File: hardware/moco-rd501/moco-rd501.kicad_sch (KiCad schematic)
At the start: 34 parts, among them J1 Conn_01x06, J2 Debug, J3 Conn_01x02, J4 Conn_01x09, SW1 SW_Push, SW2 SW_Push, U1 XC6220B331MR

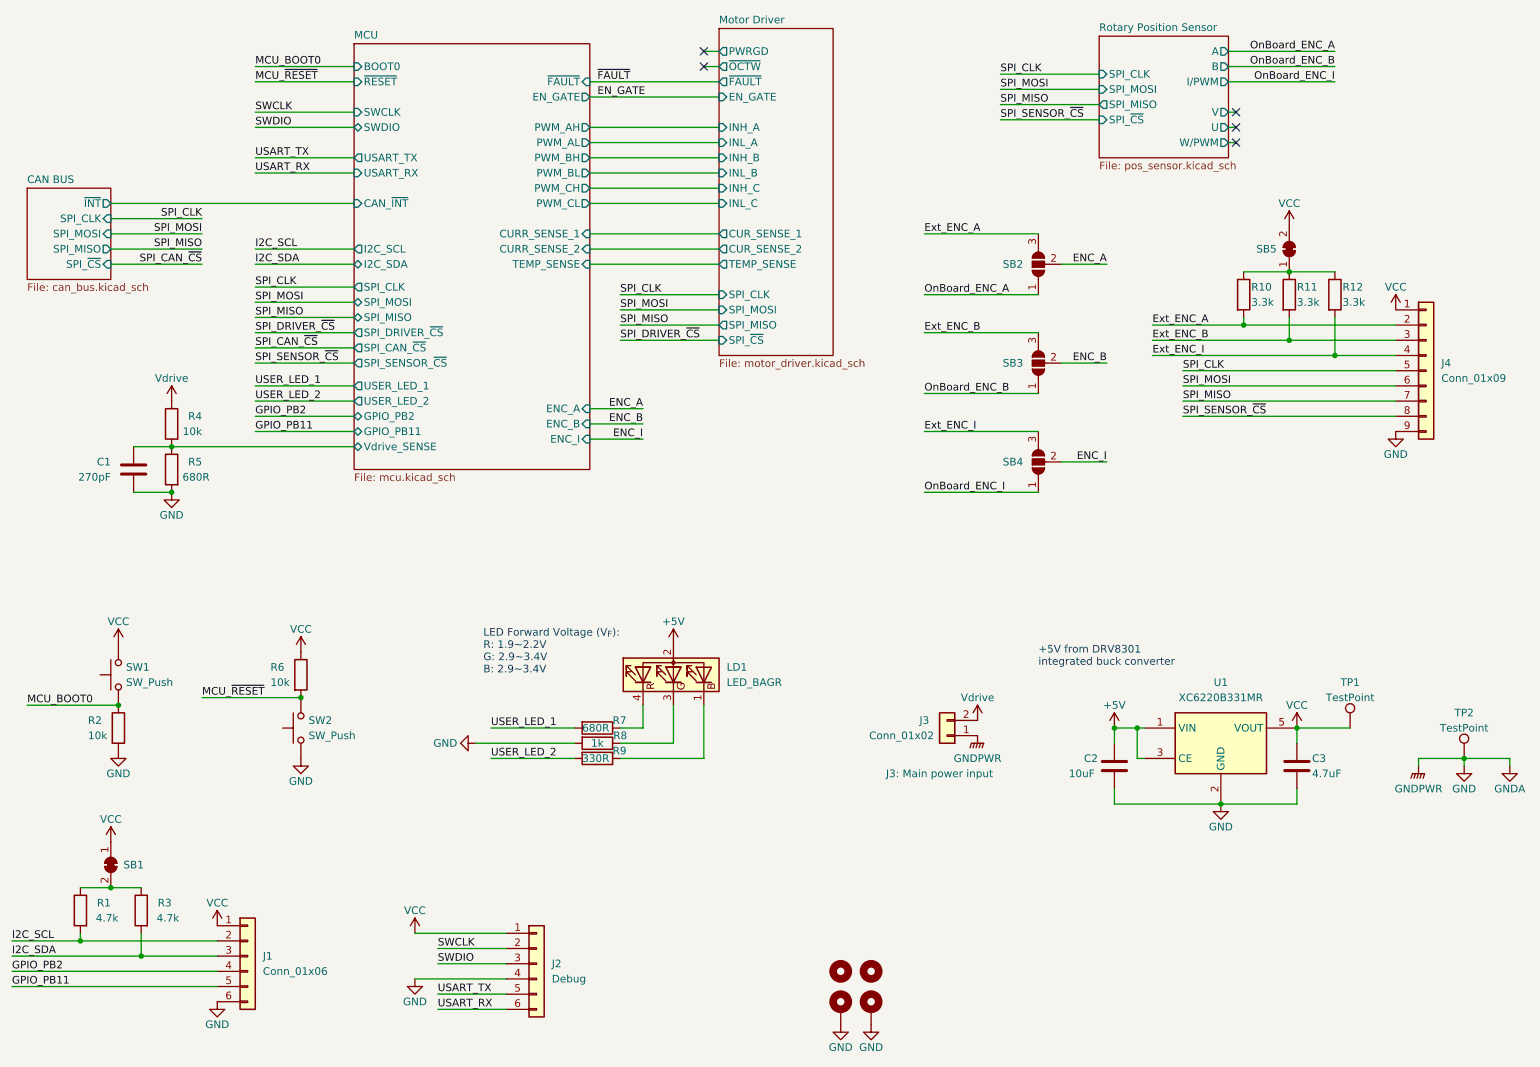
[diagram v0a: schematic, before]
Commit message: Rename "moco-s" to "moco-rd501"
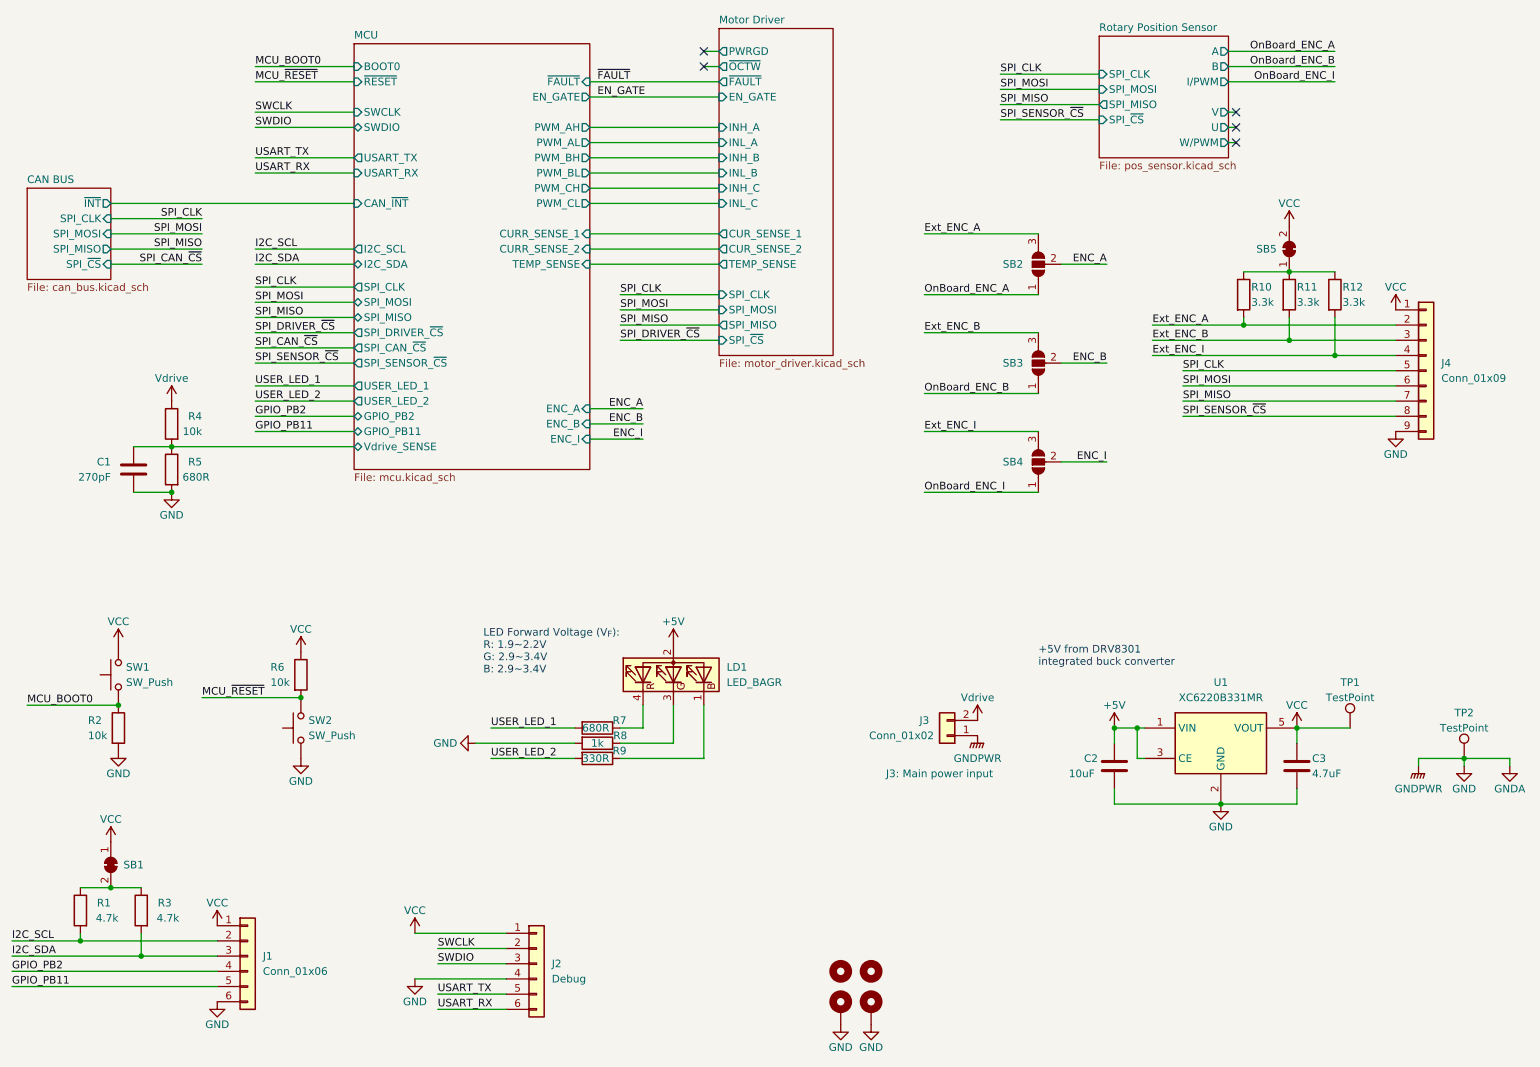
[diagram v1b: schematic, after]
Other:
- title: moco-s -> moco-RD501
